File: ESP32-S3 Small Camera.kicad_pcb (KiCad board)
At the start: 6 copper layers, 70 x 70 mm, 93 parts, among them J1 Conn_01x24, J2 U.FL Antenna Conn, J3 Conn_01x08, J4 Test Pad RST BOOT, Q1 FS8205A, U1 TLV73328PDQNR, U10 TLV73328PDQNR, U11 SN74LVC1T45DCK, U12 SN74LVC1T45DCK, U13 SN74LVC1T45DCK, U2 USBLC6-2SC6, U3 BQ25180YBGR, U4 TPS62840YBGR, U5 BQ27441-G1, U6 DW01A, U7 W25Q128JVP, U8 ESP32-S3R8, U9 TLV73315PDQNR, X1 40MHz, 15pF

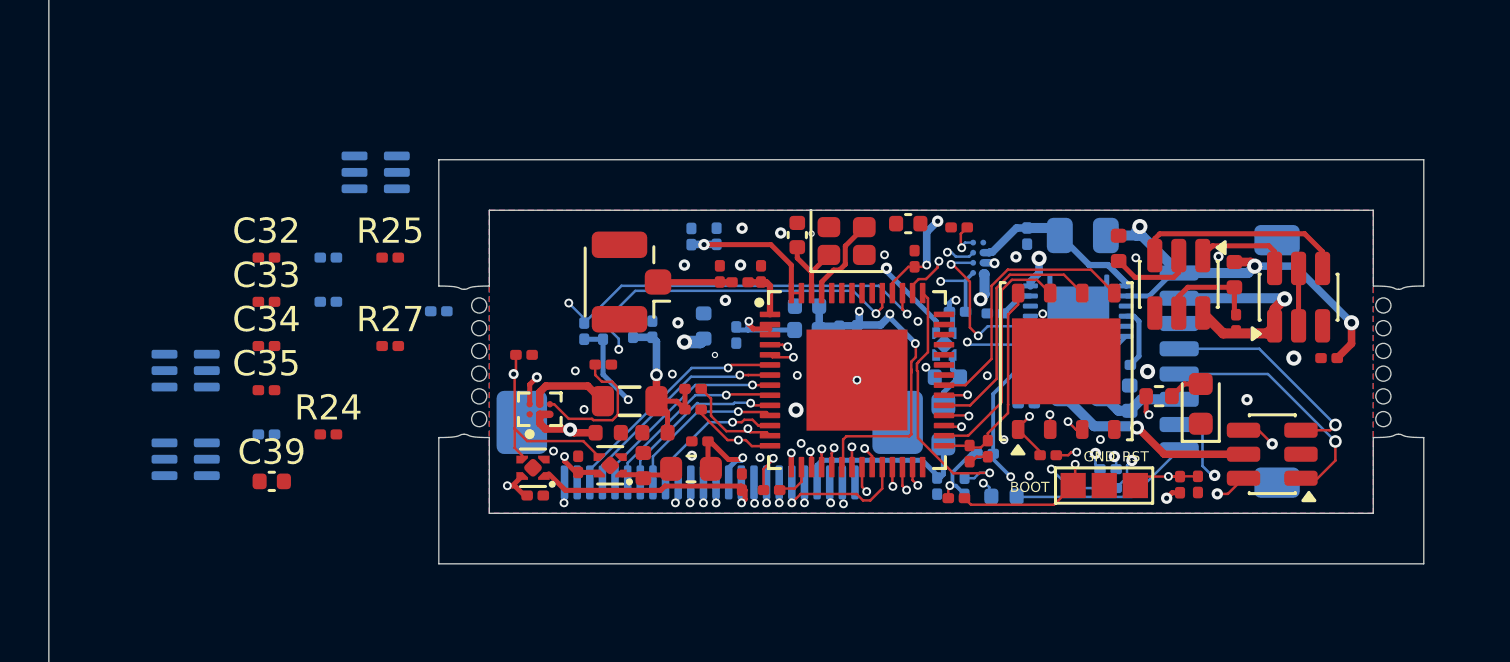
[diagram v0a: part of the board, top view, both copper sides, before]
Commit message: PCB Layout
Switched from 6 -> 8 layers
Routed and placed all components
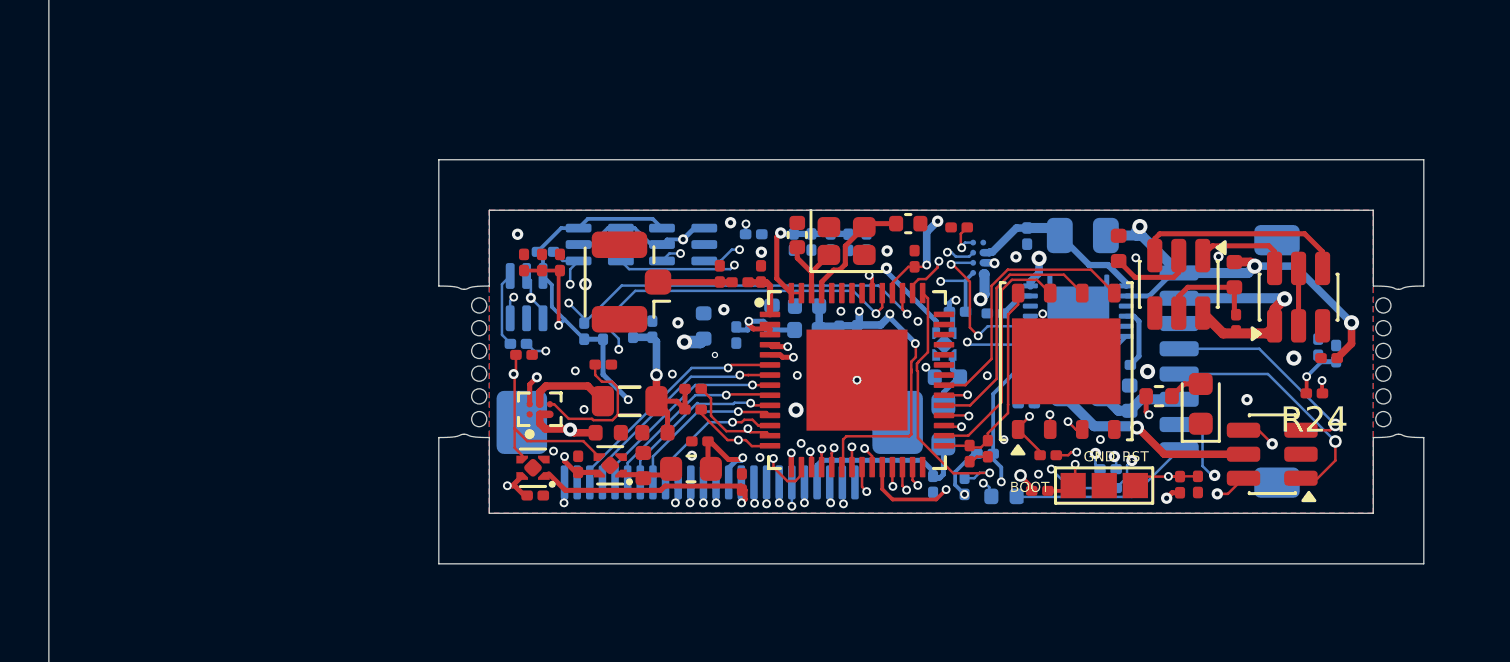
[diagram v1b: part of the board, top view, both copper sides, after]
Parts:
- C32, C33, C34, C35, C39, R17, R25, R27: moved to B.Cu
- C36, C37, C38: moved to F.Cu
- moved C32 41.8 mm to (166.3, 93.4), turned to 90 degrees
- moved R24 39.1 mm to (166.2, 95.2), turned to 180 degrees
- moved R25 37.6 mm to (167.0, 93.7), turned to 90 degrees
- moved C33 22.5 mm to (147.0, 89.3), turned to -90 degrees
- moved C34 22.0 mm to (146.3, 89.3), turned to -90 degrees
- moved C35 21.7 mm to (145.6, 89.3), turned to -90 degrees
- moved U13 21.5 mm to (141.2, 89.4)
- moved C39 20.8 mm to (144.7, 92.3), turned to -90 degrees
- moved U12 17.1 mm to (137.9, 89.4)
- moved R27 15.1 mm to (144.0, 89.0), turned to 180 degrees
- moved C36 13.5 mm to (136.3, 90.1), turned to -90 degrees
- moved R17 11.6 mm to (134.7, 93.3), turned to 180 degrees
- moved C37 8.46 mm to (135.6, 90.1), turned to -90 degrees
- moved C38 7.90 mm to (134.9, 90.1), turned to -90 degrees
- moved U11 7.75 mm to (135.0, 91.4), turned to 90 degrees
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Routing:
- net VBUS_SENSE: track 0.00 -> 22.5 mm, vias 0 -> 2
- net CAM_EN: track 15.9 -> 36.0 mm
- net RST_CM_CAM: track 0.00 -> 19.7 mm, vias 0 -> 3
- net RESET: track 3.86 -> 22.6 mm
- net RST_CM_3V3: track 0.00 -> 18.2 mm, vias 0 -> 2
- net PWDN_CAM: track 0.00 -> 17.8 mm, vias 0 -> 2
- net MCLK_3V3: track 0.00 -> 16.2 mm, vias 0 -> 2
- net VBUS: track 19.4 -> 35.1 mm, vias 2 -> 3
- net PWDN_3V3: track 0.00 -> 14.5 mm, vias 0 -> 2
- net DOVDD: track 13.2 -> 27.0 mm, vias 2 -> 3
- net BOOT: track 6.57 -> 20.2 mm
- net (no net): track 13.0 -> 0.00 mm, vias 3 -> 0
- net VCC_3V3: track 42.6 -> 51.4 mm, vias 16 -> 22
- net MCLK_CAM: track 5.67 -> 10.5 mm
- net Net-(U11-B): track 0.00 -> 2.96 mm
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- added copper zone on In3.Cu, net GND
- added copper zone on In5.Cu, net GND
- added copper zone on In6.Cu, net GND
- added copper zone on In4.Cu, net VCC_3V3
- removed copper zone on In4.Cu, net GND
- removed copper zone on In3.Cu, net VCC_3V3
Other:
- copper layers 6 -> 8

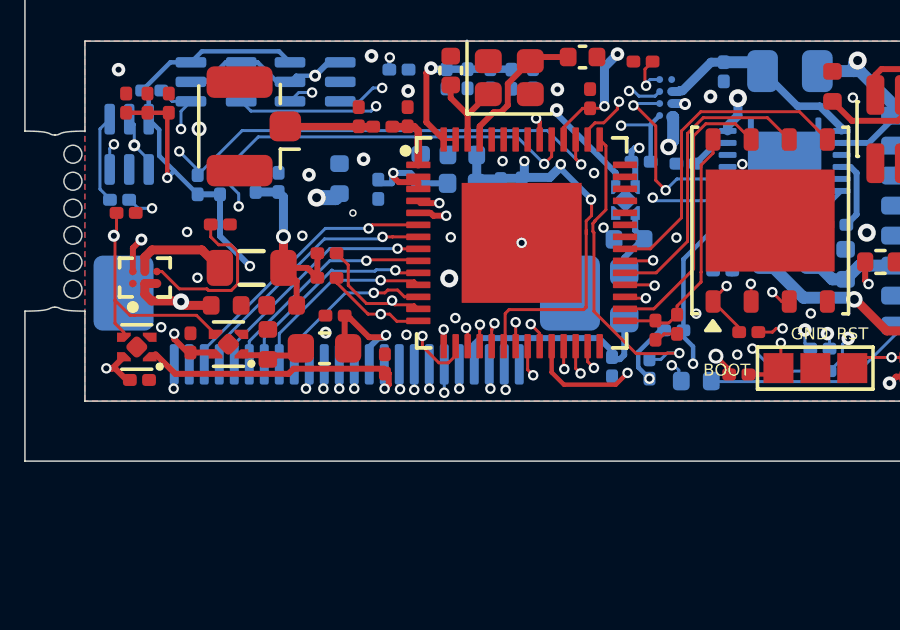
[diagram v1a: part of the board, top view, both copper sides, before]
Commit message: Fixed bugs, rerouted ln.5 track
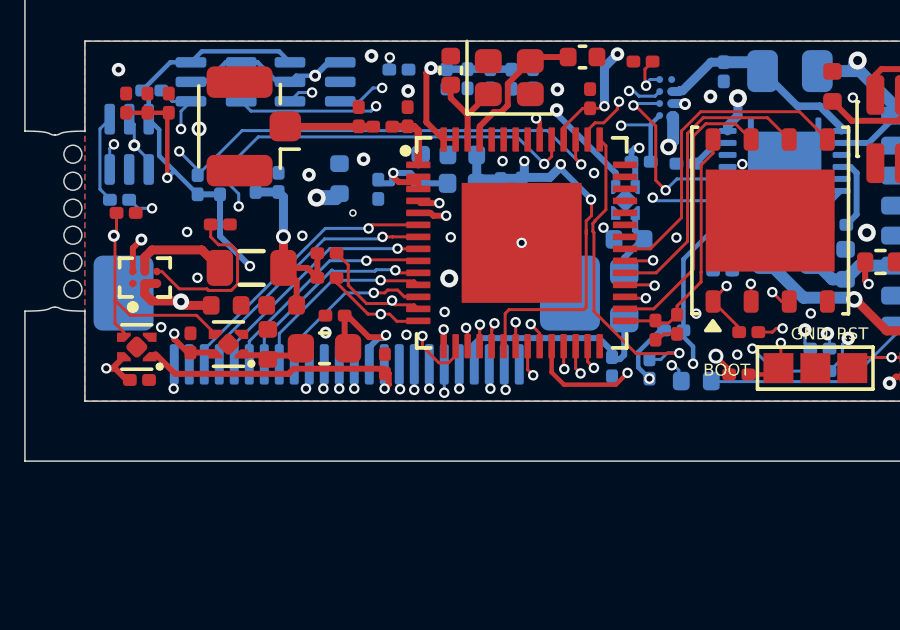
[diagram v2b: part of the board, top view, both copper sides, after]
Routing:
- net RST_CM_CAM: track 19.7 -> 17.6 mm

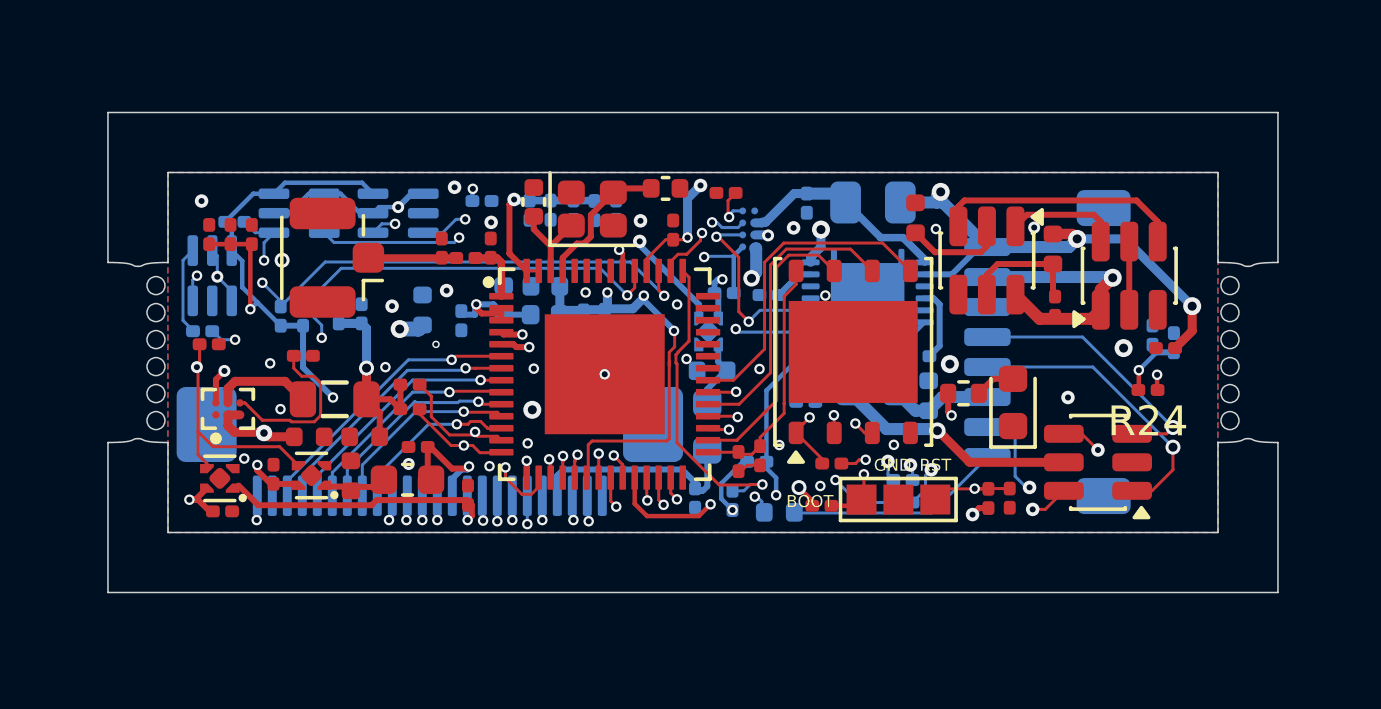
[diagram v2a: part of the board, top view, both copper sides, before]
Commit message: Rerouted, cleaned up
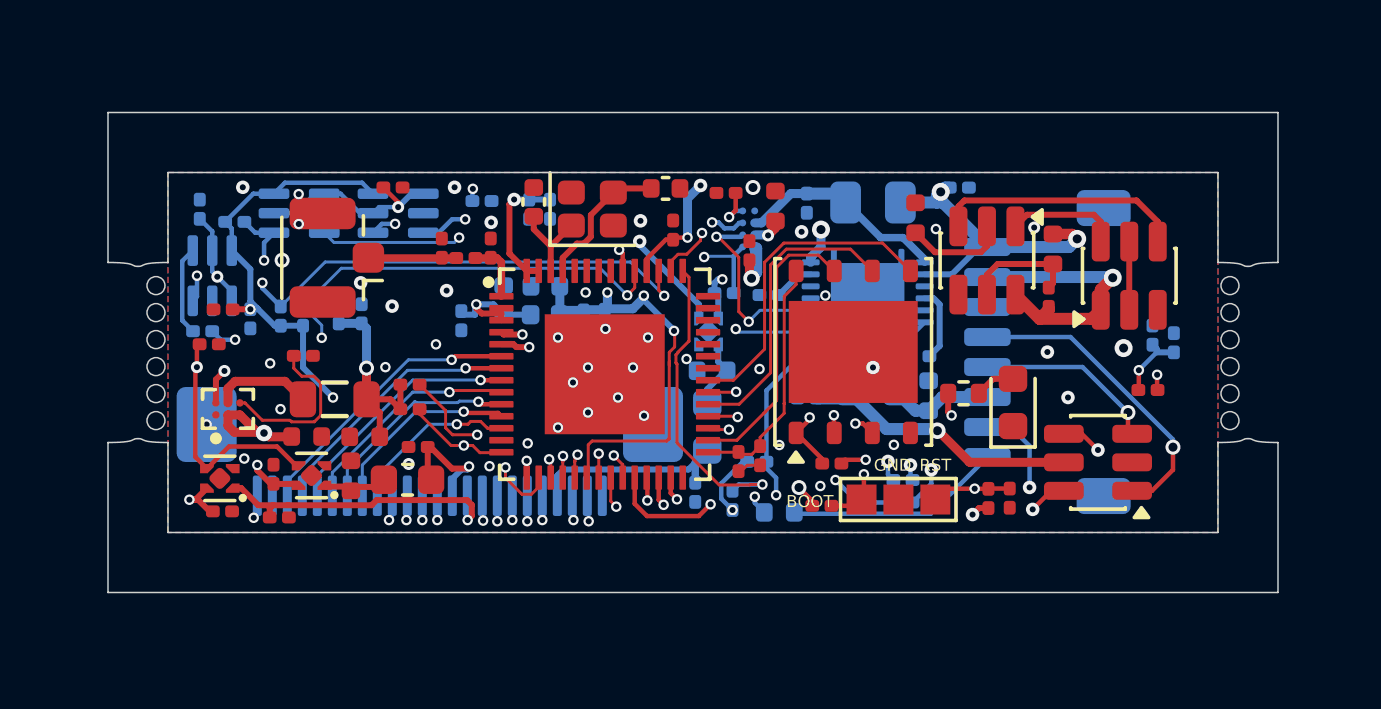
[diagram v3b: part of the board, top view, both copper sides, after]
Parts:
- removed C35, C38: 100nF, Capacitor_SMD:C_0201_0603Metric
- C10, C34, C9: moved to F.Cu
- C36, C7: moved to B.Cu
- moved C33 12.5 mm to (134.6, 89.2), turned to 90 degrees
- moved C10 12.3 mm to (153.7, 89.1)
- moved C7 8.71 mm to (159.9, 88.5), turned to 180 degrees
- moved C24 6.33 mm to (137.2, 99.5), turned to 0 degrees
- moved C34 5.31 mm to (141.0, 88.5), turned to 0 degrees
- moved C9 4.69 mm to (152.9, 90.6), turned to -90 degrees
- moved C36 2.81 mm to (136.2, 92.9), turned to 90 degrees
- moved C37 2.51 mm to (135.3, 92.6), turned to 0 degrees
- moved C25 2.20 mm to (146.2, 89.2)
- moved C26 2.18 mm to (145.5, 89.2)
- moved C8 0.36 mm to (162.9, 92.2)
- moved C22 0.19 mm to (151.1, 98.7)
- moved C2 0.12 mm to (154.8, 95.5)
- moved C11 0.08 mm to (138.1, 96.8)
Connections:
- J3 pad 4: D+X -> D-X
- J3 pad 5: D-X -> D+X
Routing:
- net B+: track 22.7 -> 16.7 mm, vias 4 -> 3
- net SDA: track 27.6 -> 23.6 mm
- net DOVDD: track 27.0 -> 24.0 mm
- net D+X: track 8.88 -> 6.08 mm
- net DVDD: track 9.56 -> 10.2 mm
- net LOAD_SYS: track 24.8 -> 25.4 mm, vias 3 -> 2
- net D-X: track 9.70 -> 10.3 mm
- net B-: track 9.18 -> 9.70 mm
- net VCC_3V3: track 51.4 -> 51.3 mm, vias 22 -> 18
- net GND: vias 31 -> 47

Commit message: Finalize PCB
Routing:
- net SDA: track 23.6 -> 24.5 mm
- net GND: vias 47 -> 54
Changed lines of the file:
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@@
 	(generator_version "10.0")
 	(general
-		(thickness 1.6)
+		(thickness 1.199998)
 		(legacy_teardrops no)
 	)
@@
 			(layer "dielectric 2"
 				(type "core")
-				(thickness 0.3)
+				(thickness 0.166666)
 				(material "FR4")
 				(epsilon_r 4.5)
@@
 			(layer "dielectric 4"
 				(type "core")
-				(thickness 0.3)
+				(thickness 0.166666)
 				(material "FR4")
 				(epsilon_r 4.5)
@@
 			(layer "dielectric 6"
 				(type "core")
-				(thickness 0.3)
+				(thickness 0.166666)
 				(material "FR4")
 				(epsilon_r 4.5)
@@
 		(capping no)
 		(filling no)
+		(zone_defaults)
 		(pcbplotparams
 			(layerselection 0x00000000_00000000_55555555_5755f5ff)
@@
 	)
 	(via
+		(at 163.145095 99.404825)
+		(size 0.35)
+		(drill 0.2)
+		(layers "F.Cu" "B.Cu")
+		(free yes)
+		(capping no)
+		(covering
+			(front no)
+			(back no)
+		)
+		(plugging
+			(front no)
+			(back no)
+		)
+		(filling no)
+		(net "GND")
+	)
+	(via
+		(at 167.25 96)
+		(size 0.45)
+		(drill 0.2)
+		(layers "F.Cu" "B.Cu")
+		(free yes)
+		(capping no)
+		(covering
+			(front no)
+			(back no)
+		)
+		(plugging
+			(front no)
+			(back no)
+		)
+		(filling no)
+		(net "GND")
+	)
+	(via
 		(at 147.4216 91.9988)
 		(size 0.35)
@@
 	)
 	(via
+		(at 167.25 92.5)
+		(size 0.45)
+		(drill 0.2)
+		(layers "F.Cu" "B.Cu")
+		(free yes)
+		(capping no)
+		(covering
+			(front no)
+			(back no)
+		)
+		(plugging
+			(front no)
+			(back no)
+		)
+		(filling no)
+		(net "GND")
+	)
+	(via
 		(at 136.0424 97.536)
 		(size 0.35)
@@
 	)
 	(via
+		(at 134 94)
+		(size 0.35)
+		(drill 0.2)
+		(layers "F.Cu" "B.Cu")
+		(free yes)
+		(capping no)
+		(covering
+			(front no)
+			(back no)
+		)
+		(plugging
+			(front no)
+			(back no)
+		)
+		(filling no)
+		(net "GND")
+	)
+	(via
 		(at 148.082016 93.21407)
 		(size 0.35)
@@
 	(via
 		(at 137.304428 90.92484)
-		(size 0.5)
-		(drill 0.3)
+		(size 0.45)
+		(drill 0.2)
 		(layers "F.Cu" "B.Cu")
 		(free yes)
@@
 	)
 	(via
+		(at 163 88.5)
+		(size 0.35)
+		(drill 0.2)
+		(layers "F.Cu" "B.Cu")
+		(free yes)
+		(capping no)
+		(covering
+			(front no)
+			(back no)
+		)
+		(plugging
+			(front no)
+			(back no)
+		)
+		(filling no)
+		(net "GND")
+	)
+	(via
 		(at 140.97 92.456)
 		(size 0.45)
@@
 	(via
 		(at 153 88.5)
-		(size 0.5)
-		(drill 0.3)
+		(size 0.45)
+		(drill 0.2)
 		(layers "F.Cu" "B.Cu")
 		(free yes)
@@
 	)
 	(via
+		(at 163.75 92.25)
+		(size 0.35)
+		(drill 0.2)
+		(layers "F.Cu" "B.Cu")
+		(free yes)
+		(capping no)
+		(covering
+			(front no)
+			(back no)
+		)
+		(plugging
+			(front no)
+			(back no)
+		)
+		(filling no)
+		(net "GND")
+	)
+	(via
 		(at 145.4912 97.028)
 		(size 0.35)
@@
 	)
 	(via
+		(at 156.75 92.25)
+		(size 0.35)
+		(drill 0.2)
+		(layers "F.Cu" "B.Cu")
+		(free yes)
+		(capping no)
+		(covering
+			(front no)
+			(back no)
+		)
+		(plugging
+			(front no)
+			(back no)
+		)
+		(filling no)
+		(net "GND")
+	)
+	(via
 		(at 162.814 93.984389)
 		(size 0.45)
@@
 		(start 143.107762 90.850198)
 		(end 140.187938 90.850198)
-		(width 0.25)
+		(width 0.151)
 		(layer "F.Cu")
 		(net "Net-(J2-In)")
@@
 	(via
 		(at 140.117762 94.520198)
-		(size 0.5)
-		(drill 0.3)
+		(size 0.45)
+		(drill 0.2)
 		(layers "F.Cu" "B.Cu")
 		(capping no)
@@
 		(start 143.912034 90.850198)
 		(end 144.472762 90.850198)
-		(width 0.25)
+		(width 0.151)
 		(layer "F.Cu")
 		(net "Net-(U8-LNA_IN)")
@@
 		(start 144.472762 90.850198)
 		(end 144.612762 90.990198)
-		(width 0.25)
+		(width 0.151)
 		(layer "F.Cu")
 		(net "Net-(U8-LNA_IN)")
@@
 		(start 144.612762 90.990198)
 		(end 144.612762 92.125198)
-		(width 0.25)
+		(width 0.151)
 		(layer "F.Cu")
 		(net "Net-(U8-LNA_IN)")
@@
 	)
 	(segment
+		(start 143.80775 96.743)
+		(end 143.989948 96.925198)
+		(width 0.15)
+		(layer "F.Cu")
+		(net "SDA")
+	)
+	(segment
 		(start 142.754 95.936436)
 		(end 141.887762 95.070198)
@@
 	)
 	(segment
+		(start 143.989948 96.925198)
+		(end 144.612762 96.925198)
+		(width 0.15)
+		(layer "F.Cu")
+		(net "SDA")
+	)
+	(segment
 		(start 142.984025 96.743)
 		(end 142.754 96.512975)
@@
 		(polygon
 			(pts
-				(xy 133.5 88) (xy 168.5 88) (xy 168.5 100) (xy 133.5 100)
+				(xy 133.7 88) (xy 168.3 88) (xy 168.3 100) (xy 133.7 100)
 			)
 		)
@@
 		(polygon
 			(pts
-				(xy 133.5 88) (xy 133.5 100) (xy 168.5 100) (xy 168.5 88)
+				(xy 133.7 88) (xy 133.7 100) (xy 168.3 100) (xy 168.3 88)
 			)
 		)

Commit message: Manufacturing Files Updated
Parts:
- C14, C39: footprint Capacitor_SMD:C_0402_1005Metric -> PCM_JLCPCB:C_0402
- moved R15 0.36 mm to (155.3, 99.5)
- moved X1 0.09 mm to (147.6, 89.3)
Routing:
- net GND: track 1.82 -> 1.80 mm, vias 54 -> 56
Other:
- board size 70 x 70 mm -> 60 x 70 mm
